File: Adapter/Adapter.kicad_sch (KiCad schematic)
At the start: 11 parts, among them J2 Conn_01x14_Socket, U1 BGA153 UFS Modified

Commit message: V1.1
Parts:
- removed J2: Conn_01x14_Socket, BGA153:FPC 14 Pin 0.5P, symbol Connector:Conn_01x14_Socket
- added J3: Conn_01x14_Socket, BGA153:FPC 14 Pin 0.5P, symbol Connector:Conn_01x14_Socket
- U1: footprint BGA153:BGA 153 Modified -> BGA153:BGA 153 Adapter Modified; symbol BGA153:BGA153 UFS Modified -> BGA153:BGA153 UFS Adapter Modified
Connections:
- net REF_CLK: now also J3.5 (Pin_5)
- net RST_N: now also J3.6 (Pin_6)
- net RX0N: now also J3.7 (Pin_7)
- net RX0P: now also J3.8 (Pin_8)
- net RX1N: now also J3.9 (Pin_9)
- net RX1P: now also J3.10 (Pin_10)
- net TX0N: now also J3.4 (Pin_4)
- net TX0P: now also J3.3 (Pin_3)
- net TX1N: now also J3.2 (Pin_2)
- net TX1P: now also J3.1 (Pin_1)
- net VCC: now also J3.11 (Pin_11)
- net VCCQ: now also J3.13 (Pin_13)
- net VCCQ2: now also J3.12 (Pin_12)
- net VSS: now also U1.B3 (VSS), J3.14 (Pin_14); no longer U1.B13 (VSS)

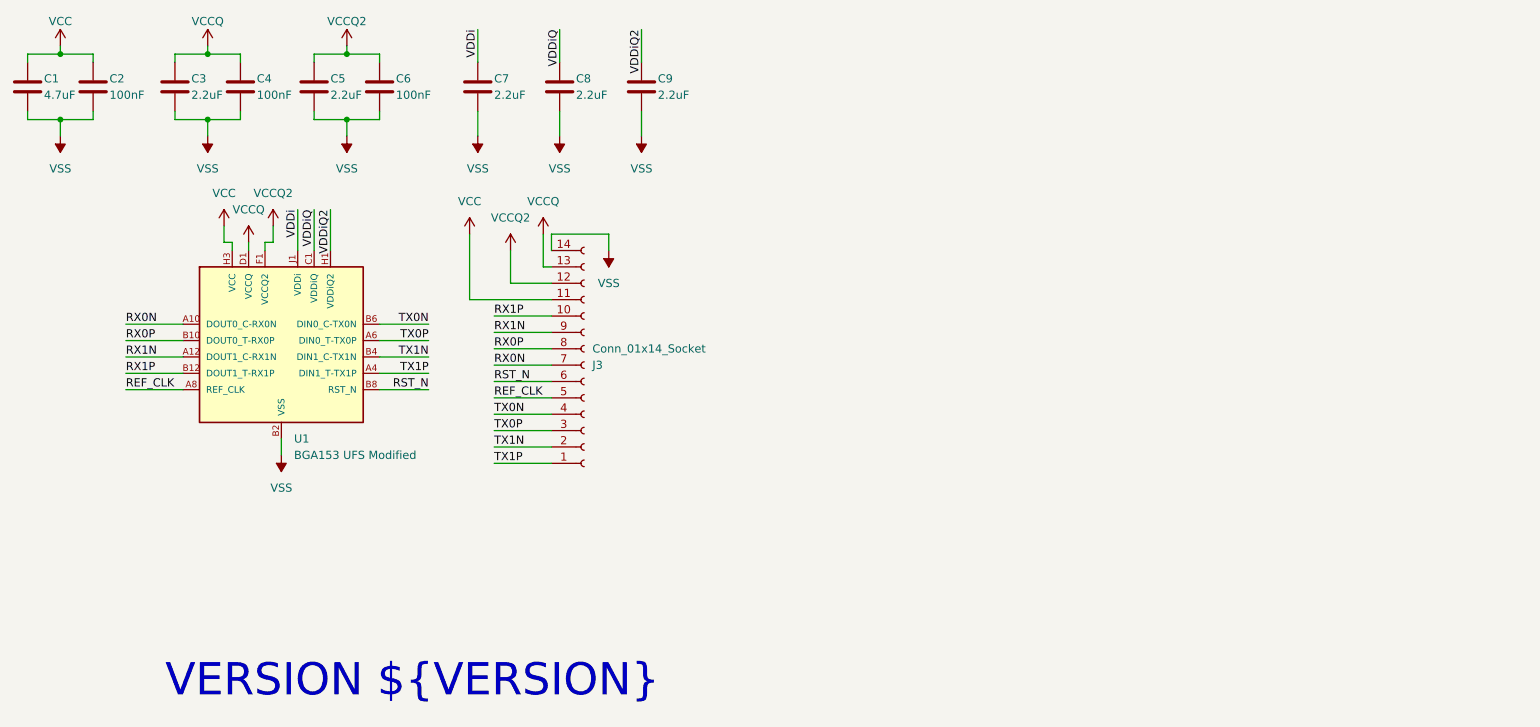
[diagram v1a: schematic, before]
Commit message: V1.2 for forward fpc cable
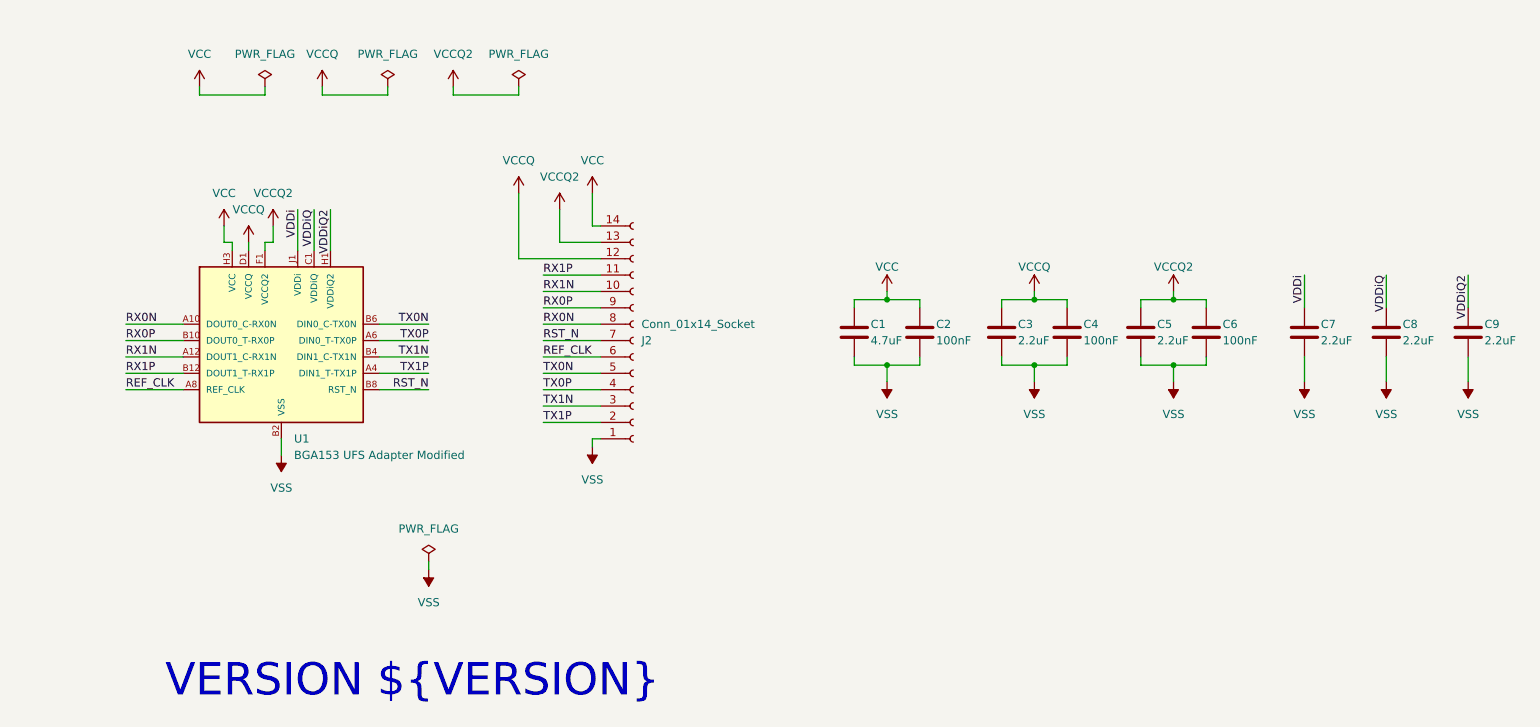
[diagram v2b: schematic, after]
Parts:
- removed J3: Conn_01x14_Socket, BGA153:FPC 14 Pin 0.5P, symbol Connector:Conn_01x14_Socket
- added J2: Conn_01x14_Socket, BGA153:FPC 14 Pin 0.5P, symbol Connector:Conn_01x14_Socket
- U1: value BGA153 UFS Modified -> BGA153 UFS Adapter Modified
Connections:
- net REF_CLK: now also J2.6 (Pin_6)
- net RST_N: now also J2.7 (Pin_7)
- net RX0N: now also J2.8 (Pin_8)
- net RX0P: now also J2.9 (Pin_9)
- net RX1N: now also J2.10 (Pin_10)
- net RX1P: now also J2.11 (Pin_11)
- net TX0N: now also J2.5 (Pin_5)
- net TX0P: now also J2.4 (Pin_4)
- net TX1N: now also J2.3 (Pin_3)
- net TX1P: now also J2.2 (Pin_2)
- net VCC: now also J2.14 (Pin_14)
- net VCCQ: now also J2.12 (Pin_12)
- net VCCQ2: now also J2.13 (Pin_13)
- net VSS: now also J2.1 (Pin_1)

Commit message: V1.3 GB042 Connector
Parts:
- removed J2: Conn_01x14_Socket, BGA153:FPC 14 Pin 0.5P, symbol Connector:Conn_01x14_Socket
- added J1: GB042-30P-H10, BGA153:GB042-30P-H10, symbol BGA153:GB042-30P-H10
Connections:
- net REF_CLK: now also J1.8 (Pin_8)
- net RST_N: now also J1.23 (Pin_23)
- net RX0N: now also J1.6 (Pin_6)
- net RX0P: now also J1.5 (Pin_5)
- net RX1N: now also J1.3 (Pin_3)
- net RX1P: now also J1.2 (Pin_2)
- net TX0N: now also J1.10 (Pin_10)
- net TX0P: now also J1.11 (Pin_11)
- net TX1N: now also J1.13 (Pin_13)
- net TX1P: now also J1.14 (Pin_14)
- net VCC: now also J1.29 (Pin_29)
- net VCCQ: now also J1.27 (Pin_27)
- net VCCQ2: now also J1.25 (Pin_25)
- net VDDi: now also J1.17 (Pin_17)
- net VDDiQ: now also J1.21 (Pin_21)
- net VDDiQ2: now also J1.19 (Pin_19)
- net VSS: now also J1.1 (Pin_1), J1.12 (Pin_12), J1.15 (Pin_15), J1.16 (Pin_16), J1.18 (Pin_18), J1.20 (Pin_20), J1.22 (Pin_22), J1.24 (Pin_24), J1.26 (Pin_26), J1.28 (Pin_28), J1.30 (Pin_30), J1.4 (Pin_4), J1.7 (Pin_7), J1.9 (Pin_9)
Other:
- moved on the sheet: C1, C2, C3, C4, C5, C6, C7, C8, C9
